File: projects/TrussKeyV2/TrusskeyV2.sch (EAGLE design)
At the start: 43 parts, among them J1 M20-9980346, J2 XF2L-0535-1, J3 10104111-0001LF, Q1 ABM-16MHZ, SW1 LS12T2-T, SW2 EVQ11U09K, SW3 ESE31L11T, U2 TPS62200, U3 LC709203, U5 MCP73831T-2ACI/OT, X1 CON-1PIN, X3 CON-1PIN

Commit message: TrussKey v2
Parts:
- removed JP2: Solenoid, jumper:JP1E
- added X2, X4: CON-1PIN, NewPart:CON-1PIN
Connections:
- net N$9: now also X4.P$1; no longer JP2.1
- net VCC: now also X2.P$1; no longer JP2.2
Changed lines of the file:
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@@
 <part name="P+2" library="supply1" deviceset="VCC" device=""/>
 <part name="GND6" library="supply1" deviceset="GND" device=""/>
-<part name="JP2" library="jumper" deviceset="JP1E" device="" value="Solenoid"/>
 <part name="P+8" library="supply1" deviceset="VCC" device=""/>
 <part name="D1" library="diode" deviceset="DIODE-" device="SOD123"/>
@@
 <part name="J1" library="M20-9980346" library_urn="urn:adsk.eagle:library:10158210" deviceset="M20-9980346" device="" package3d_urn="urn:adsk.eagle:package:10158213/3"/>
 <part name="J3" library="10104111-0001LF" library_urn="urn:adsk.eagle:library:10158429" deviceset="10104111-0001LF" device="" package3d_urn="urn:adsk.eagle:package:10158432/2"/>
+<part name="X2" library="NewPart" deviceset="CON-1PIN" device=""/>
+<part name="X4" library="NewPart" deviceset="CON-1PIN" device=""/>
 </parts>
 <sheets>
@@
 </plain>
 <instances>
-<instance part="JP2" gate="A" x="38.1" y="76.2" smashed="yes" rot="R90">
-<attribute name="NAME" x="38.1" y="74.93" size="1.778" layer="95" rot="R180"/>
-<attribute name="VALUE" x="38.1" y="81.915" size="1.778" layer="96" rot="R180"/>
-</instance>
 <instance part="P+8" gate="VCC" x="48.26" y="88.9" smashed="yes">
 <attribute name="VALUE" x="45.72" y="86.36" size="1.778" layer="96" rot="R90"/>
@@
 </instance>
 <instance part="Q2" gate="G$1" x="45.72" y="68.58" smashed="yes">
-<attribute name="NAME" x="35.56" y="76.2" size="1.778" layer="95"/>
 <attribute name="VALUE" x="35.56" y="73.66" size="1.778" layer="96"/>
 </instance>
@@
 <attribute name="NAME" x="223.52" y="86.36" size="1.778" layer="95"/>
 </instance>
+<instance part="X2" gate="G$1" x="35.56" y="78.74" smashed="yes" rot="R180"/>
+<instance part="X4" gate="G$1" x="35.56" y="76.2" smashed="yes" rot="R180"/>
 </instances>
 <busses>
@@
 <net name="VCC" class="0">
 <segment>
-<pinref part="JP2" gate="A" pin="2"/>
 <pinref part="P+8" gate="VCC" pin="VCC"/>
 <wire x1="40.64" y1="78.74" x2="48.26" y2="78.74" width="0.1524" layer="91"/>
@@
 <wire x1="58.42" y1="83.82" x2="48.26" y2="83.82" width="0.1524" layer="91"/>
 <junction x="48.26" y="83.82"/>
+<pinref part="X2" gate="G$1" pin="P$1"/>
 </segment>
 <segment>
@@
 <net name="N$9" class="0">
 <segment>
-<pinref part="JP2" gate="A" pin="1"/>
 <pinref part="Q2" gate="G$1" pin="C"/>
 <wire x1="40.64" y1="76.2" x2="48.26" y2="76.2" width="0.1524" layer="91"/>
@@
 <wire x1="58.42" y1="73.66" x2="48.26" y2="73.66" width="0.1524" layer="91"/>
 <junction x="48.26" y="73.66"/>
-</segment>
-</net>
+<pinref part="X4" gate="G$1" pin="P$1"/>
+</segment>
+</net>

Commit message: V2 PCB
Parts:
- removed X2, X4: CON-1PIN, NewPart:CON-1PIN
- added J4, J5: 5-146280-1, 5-146280-1:5-146280-1
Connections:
- net N$9: now also J5.1; no longer X4.P$1
- net VCC: now also J4.1; no longer X2.P$1
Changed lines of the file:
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@@
 <part name="J1" library="M20-9980346" library_urn="urn:adsk.eagle:library:10158210" deviceset="M20-9980346" device="" package3d_urn="urn:adsk.eagle:package:10158213/3"/>
 <part name="J3" library="10104111-0001LF" library_urn="urn:adsk.eagle:library:10158429" deviceset="10104111-0001LF" device="" package3d_urn="urn:adsk.eagle:package:10158432/2"/>
-<part name="X2" library="NewPart" deviceset="CON-1PIN" device=""/>
-<part name="X4" library="NewPart" deviceset="CON-1PIN" device=""/>
+<part name="J4" library="5-146280-1" deviceset="5-146280-1" device=""/>
+<part name="J5" library="5-146280-1" deviceset="5-146280-1" device=""/>
 </parts>
 <sheets>
@@
 <attribute name="NAME" x="223.52" y="86.36" size="1.778" layer="95"/>
 </instance>
-<instance part="X2" gate="G$1" x="35.56" y="78.74" smashed="yes" rot="R180"/>
-<instance part="X4" gate="G$1" x="35.56" y="76.2" smashed="yes" rot="R180"/>
+<instance part="J4" gate="G$1" x="38.1" y="83.82" smashed="yes" rot="R180">
+<attribute name="NAME" x="21.59" y="76.2" size="1.778" layer="95" rot="R180" align="center-left"/>
+<attribute name="VALUE" x="21.59" y="78.74" size="1.778" layer="96" rot="R180" align="center-left"/>
+</instance>
+<instance part="J5" gate="G$1" x="38.1" y="76.2" smashed="yes" rot="R180">
+<attribute name="NAME" x="21.59" y="68.58" size="1.778" layer="95" rot="R180" align="center-left"/>
+<attribute name="VALUE" x="21.59" y="71.12" size="1.778" layer="96" rot="R180" align="center-left"/>
+</instance>
 </instances>
 <busses>
@@
 <segment>
 <pinref part="P+8" gate="VCC" pin="VCC"/>
-<wire x1="40.64" y1="78.74" x2="48.26" y2="78.74" width="0.1524" layer="91"/>
-<wire x1="48.26" y1="78.74" x2="48.26" y2="83.82" width="0.1524" layer="91"/>
+<wire x1="38.1" y1="83.82" x2="48.26" y2="83.82" width="0.1524" layer="91"/>
 <pinref part="D1" gate="G$1" pin="C"/>
 <wire x1="48.26" y1="83.82" x2="48.26" y2="86.36" width="0.1524" layer="91"/>
@@
 <wire x1="58.42" y1="83.82" x2="48.26" y2="83.82" width="0.1524" layer="91"/>
 <junction x="48.26" y="83.82"/>
-<pinref part="X2" gate="G$1" pin="P$1"/>
+<pinref part="J4" gate="G$1" pin="1"/>
 </segment>
 <segment>
@@
 <segment>
 <pinref part="Q2" gate="G$1" pin="C"/>
-<wire x1="40.64" y1="76.2" x2="48.26" y2="76.2" width="0.1524" layer="91"/>
+<wire x1="38.1" y1="76.2" x2="48.26" y2="76.2" width="0.1524" layer="91"/>
 <wire x1="48.26" y1="76.2" x2="48.26" y2="73.66" width="0.1524" layer="91"/>
 <pinref part="D1" gate="G$1" pin="A"/>
@@
 <wire x1="58.42" y1="73.66" x2="48.26" y2="73.66" width="0.1524" layer="91"/>
 <junction x="48.26" y="73.66"/>
-<pinref part="X4" gate="G$1" pin="P$1"/>
-</segment>
-</net>
+<pinref part="J5" gate="G$1" pin="1"/>
+</segment>
+</net>

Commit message: FPC changed
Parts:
- removed J2: XF2L-0535-1, adafruit:XF2L-0535-1
- added J6: MOLEX_503480-0600MOLEX_503480-0600_0_0, Molex - 503480-0600:MOLEX_503480-0600MOLEX_503480-0600_0_0
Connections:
- net GND: now also J6.5; no longer J2-5.MS
- net REST: now also J6.2; no longer J2-2.MS
- net RX: now also J6.4; no longer J2-4.MS
- net TX: now also J6.3; no longer J2-3.MS
- net VCC: now also J6.1; no longer J2-1.MSV
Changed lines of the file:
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@@
 <part name="U1" library="SparkFun-DigitalIC" deviceset="ATMEGA328P_MLF" device="MLF32"/>
 <part name="Q1" library="NewPart" deviceset="ABM-16MHZ" device=""/>
-<part name="J2" library="adafruit" deviceset="XF2*-05?" device="35-1" technology="L"/>
 <part name="SW3" library="NewPart" deviceset="ESE31L11T" device=""/>
 <part name="SW2" library="NewPart" deviceset="EVQ11U09K" device=""/>
@@
 <part name="J4" library="5-146280-1" deviceset="5-146280-1" device=""/>
 <part name="J5" library="5-146280-1" deviceset="5-146280-1" device=""/>
+<part name="J6" library="Molex - 503480-0600" deviceset="MOLEX_503480-0600" device="MOLEX_503480-0600_0_0"/>
 </parts>
 <sheets>
@@
 <attribute name="VALUE" x="99.06" y="81.661" size="1.778" layer="96"/>
 </instance>
-<instance part="J2" gate="-1" x="162.56" y="99.06" smashed="yes">
-<attribute name="VALUE" x="162.56" y="100.33" size="1.778" layer="96"/>
-<attribute name="NAME" x="165.1" y="98.298" size="1.524" layer="95"/>
-</instance>
-<instance part="J2" gate="-2" x="162.56" y="96.52" smashed="yes">
-<attribute name="NAME" x="165.1" y="95.758" size="1.524" layer="95"/>
-</instance>
-<instance part="J2" gate="-3" x="162.56" y="93.98" smashed="yes">
-<attribute name="NAME" x="165.1" y="93.218" size="1.524" layer="95"/>
-</instance>
-<instance part="J2" gate="-4" x="162.56" y="91.44" smashed="yes">
-<attribute name="NAME" x="165.1" y="90.678" size="1.524" layer="95"/>
-</instance>
-<instance part="J2" gate="-5" x="162.56" y="88.9" smashed="yes">
-<attribute name="NAME" x="165.1" y="88.138" size="1.524" layer="95"/>
-</instance>
 <instance part="GND12" gate="1" x="109.22" y="5.08" smashed="yes">
 <attribute name="VALUE" x="106.68" y="2.54" size="1.778" layer="96"/>
@@
 <attribute name="NAME" x="21.59" y="68.58" size="1.778" layer="95" rot="R180" align="center-left"/>
 <attribute name="VALUE" x="21.59" y="71.12" size="1.778" layer="96" rot="R180" align="center-left"/>
+</instance>
+<instance part="J6" gate="G$0" x="175.26" y="101.6" smashed="yes" rot="R270">
+<attribute name="NAME" x="172.72" y="101.6" size="2.54" layer="95" rot="R270" align="top-left"/>
 </instance>
 </instances>
@@
 </segment>
 <segment>
-<pinref part="J2" gate="-1" pin="MSV"/>
 <wire x1="160.02" y1="99.06" x2="147.32" y2="99.06" width="0.1524" layer="91"/>
 <label x="147.32" y="99.06" size="1.778" layer="95"/>
+<pinref part="J6" gate="G$0" pin="1"/>
 </segment>
 <segment>
@@
 </segment>
 <segment>
-<pinref part="J2" gate="-5" pin="MS"/>
 <wire x1="160.02" y1="88.9" x2="147.32" y2="88.9" width="0.1524" layer="91"/>
 <label x="144.78" y="88.9" size="1.778" layer="95"/>
+<pinref part="J6" gate="G$0" pin="5"/>
 </segment>
 <segment>
@@
 <wire x1="160.02" y1="96.52" x2="147.32" y2="96.52" width="0.1524" layer="91"/>
 <label x="147.32" y="96.52" size="1.778" layer="95" rot="R180"/>
-<pinref part="J2" gate="-2" pin="MS"/>
+<pinref part="J6" gate="G$0" pin="2"/>
 </segment>
 </net>
@@
 <net name="RX" class="0">
 <segment>
-<pinref part="J2" gate="-4" pin="MS"/>
 <wire x1="160.02" y1="91.44" x2="147.32" y2="91.44" width="0.1524" layer="91"/>
 <label x="147.32" y="91.44" size="1.778" layer="95"/>
+<pinref part="J6" gate="G$0" pin="4"/>
 </segment>
 </net>
 <net name="TX" class="0">
 <segment>
-<pinref part="J2" gate="-3" pin="MS"/>
 <wire x1="160.02" y1="93.98" x2="147.32" y2="93.98" width="0.1524" layer="91"/>
 <label x="147.32" y="93.98" size="1.778" layer="95"/>
-</segment>
-</net>
+<pinref part="J6" gate="G$0" pin="3"/>
+</segment>
+</net>

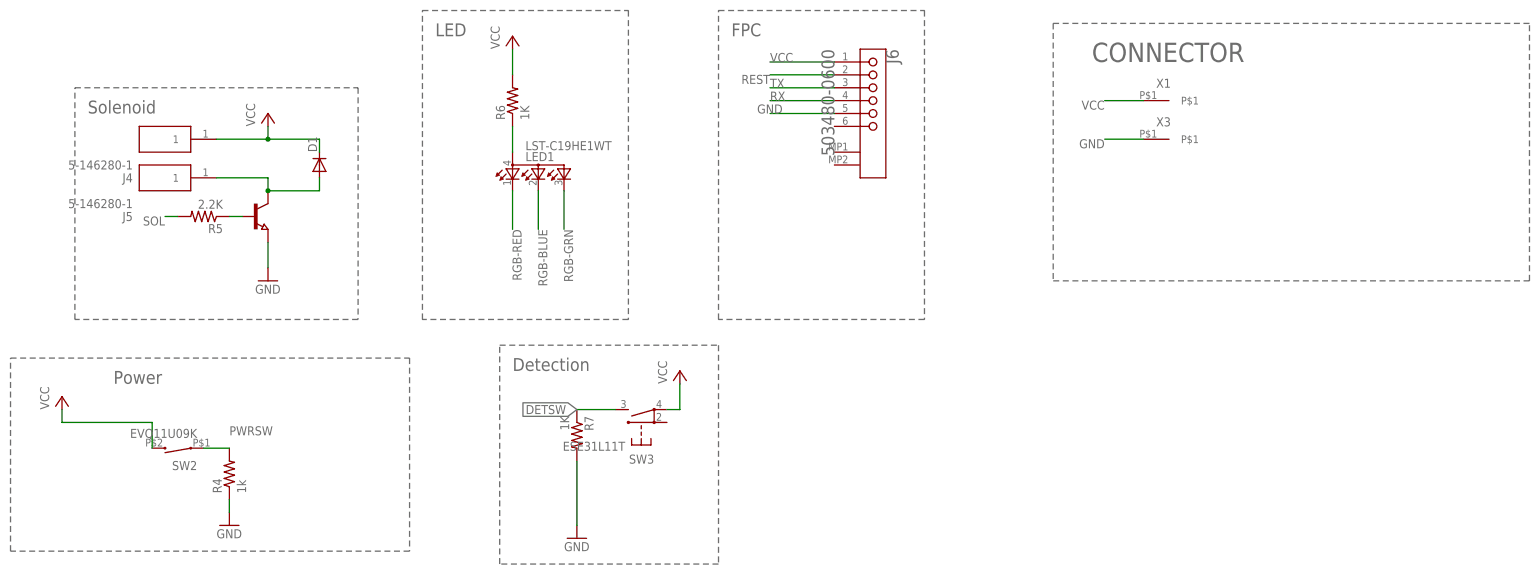
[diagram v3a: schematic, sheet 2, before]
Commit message: Gas Gauge change
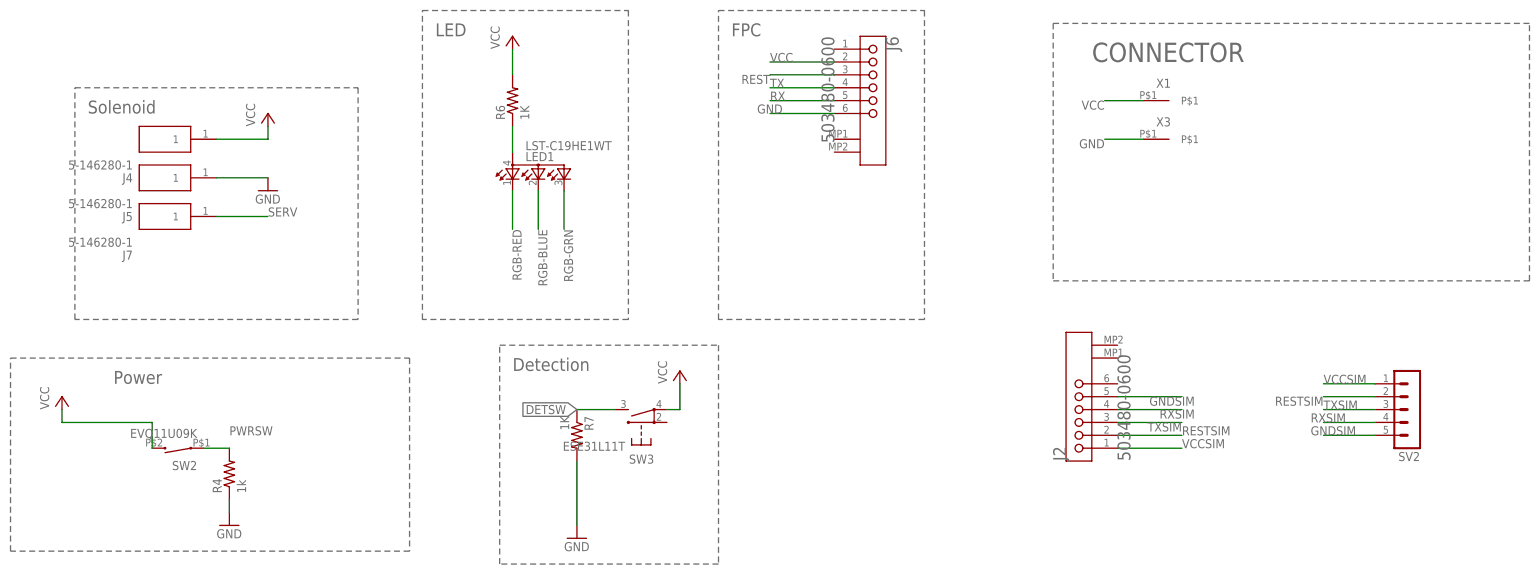
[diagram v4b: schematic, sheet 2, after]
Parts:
- removed D1: (no value), diode:DIODE-SOD123
- removed Q2: (no value), semicon-smd-ipc:NPN-TRANSISTOR_SOT23
- removed R5: 2.2K, resistor:R-US_R0402
- added J2: MOLEX_503480-0600MOLEX_503480-0600_0_0, Molex - 503480-0600:MOLEX_503480-0600MOLEX_503480-0600_0_0
- added J7: 5-146280-1, 5-146280-1:5-146280-1
- added SV2: (no value), con-lstb:MA05-1
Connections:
- removed net N$10: Q2.B, R5.1
- removed net N$7: C6.1, U2.IN
- removed net N$9: D1.A, J5.1, Q2.C
- removed net SOL: R5.2, U1.ADC6
- new net GNDSIM: J2.5, SV2.5
- new net RESTSIM: J2.2, SV2.2
- new net RXSIM: J2.4, SV2.4
- new net SERV: J7.1, U1.ADC6
- new net TXSIM: J2.3, SV2.3
- new net VCCSIM: J2.1, SV2.1
- net GND: now also J5.1, J6.6; no longer J6.5, Q2.E
- net REST: now also J6.3; no longer J6.2
- net RX: now also J6.5; no longer J6.4
- net TX: now also J6.4; no longer J6.3
- net VCC: now also C6.1, J6.2, U2.IN; no longer D1.C, J6.1
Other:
- moved on the sheet: J6

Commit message: GasGauge
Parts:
- removed C17: 1uF, rcl:C-EUC0603
- removed R15, R16: 10K, resistor:R-US_R0402
- removed U3: LC709203, NewPart:LC709203
- added C10: 1uF, rcl:C-EUC0603
- added C11: 10nF, rcl:C-EUC0603
- added IC1: MAX17043X+T10, SamacSys_Parts:MAX17043X+T10
- added R10, R5: 4.7K, resistor:R-US_R0402
- added R11: 180, resistor:R-US_R0402
- added R9: 1K, resistor:R-US_R0402
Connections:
- new net N$10: C10.1, IC1.CELL, R9.2
- new net N$9: C11.1, IC1.VDD, R11.2
- net GND: now also C10.2, C11.2, IC1.CTG, IC1.GND, IC1.QSTRT; no longer C17.1, U3.EPAD, U3.TEST, U3.VSS
- net SCL: now also IC1.SCL, R10.1; no longer R15.1, U3.SCL
- net SDA: now also IC1.SDA, R5.1; no longer R16.1, U3.SDA
- net VCC: now also R10.2, R11.1, R5.2, R9.1; no longer C17.2, R15.2, R16.2, U3.VDD
